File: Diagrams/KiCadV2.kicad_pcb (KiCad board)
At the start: 2 copper layers, 76.4 x 52.6 mm, 150 parts, among them J1 USB_C_Receptacle_PowerOnly_6P, J3 Screw_Terminal_01x02, J4 Screw_Terminal_01x02, U1 MT3608, U10 NC7SZ157P6X, U11 NC7SZ157P6X, U12 NC7SZ157P6X, U13 NC7SZ157P6X, U14 74LV08AT14-13, U15 HIP4080A, U16 NC7SZ157P6X, U17 MX3502S, U18 MX3502S, U19 NC7SZ157P6X, U2 74HC595, U20 NC7SZ157P6X, U22 DMHT10H032LFJ, U23 INA240A1D, U26 MX3502S, U3 NC7SZ157P6X, U30 DMHT10H032LFJ, U31 INA240A1D, U32 NC7SZ157P6X, U33 NC7SZ157P6X, U34 NC7SZ157P6X, U35 NC7SZ157P6X, U36 NC7SZ157P6X, U37 NC7SZ157P6X, U38 74LV08AT14-13, U39 HIP4080A, U4 NC7SZ157P6X, U40 MCP6002-xSN, U41 CJ432, U5 MX3502S, U6 NC7SZ157P6X, U7 DAC082S085CISDX/NOPB, U8 NC7SZ157P6X, U9 NC7SZ157P6X

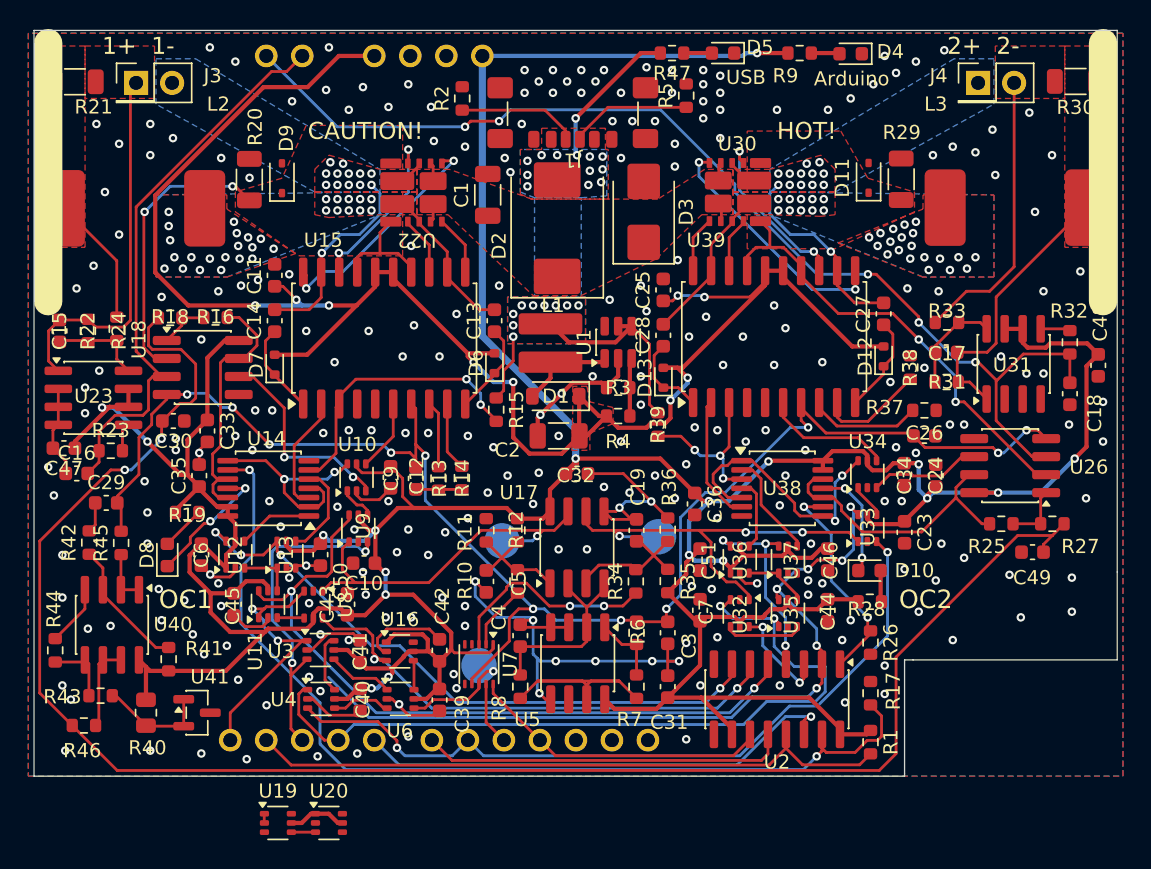
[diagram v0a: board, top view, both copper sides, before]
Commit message: Fixed AND Gate pins, added extra DAC logic Mux
DAC logic mux not yet done on PCB
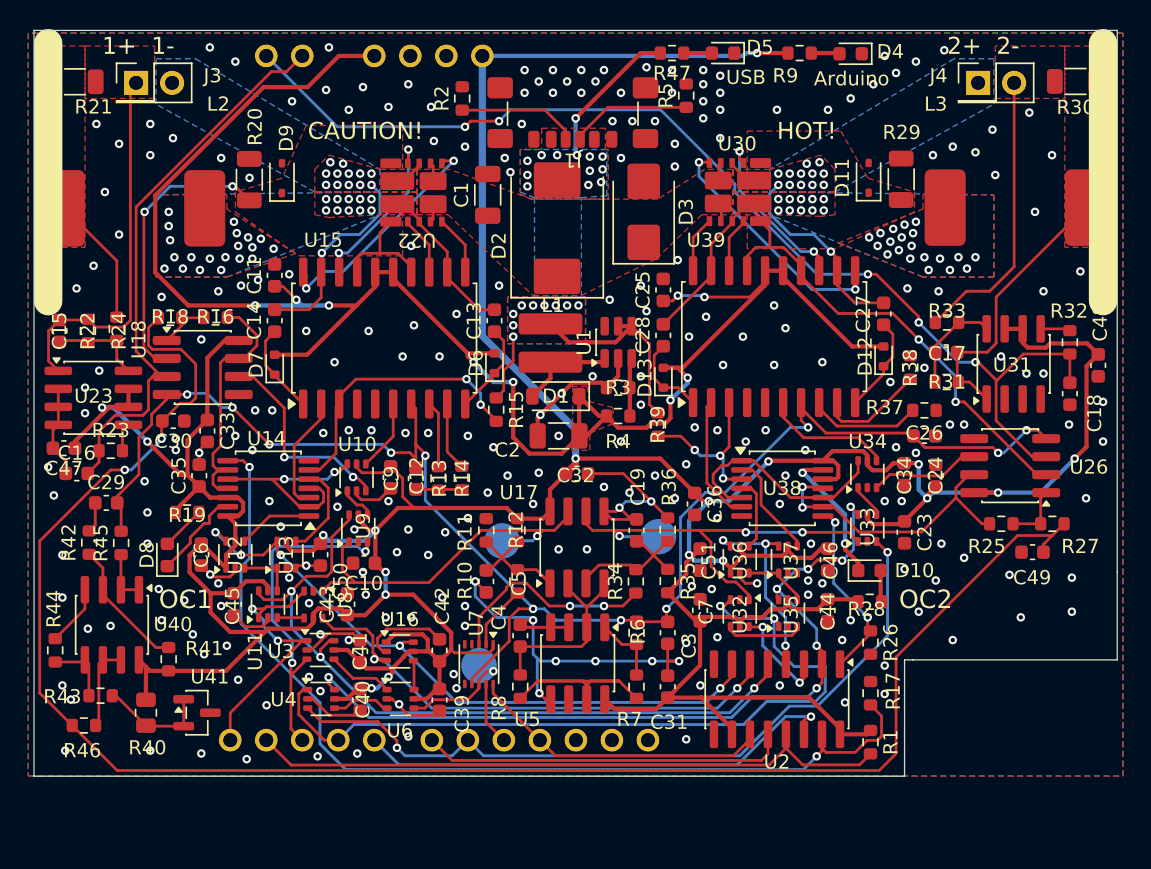
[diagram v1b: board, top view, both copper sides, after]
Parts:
- removed U19, U20: NC7SZ157P6X, Package_TO_SOT_SMD:SOT-363_SC-70-6
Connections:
- U14 pad 10: /PerCoil/~{OC1} -> /PerCoil/SignalProcessingChain/EN
- U14 pad 11: Net-(D8-K) -> /PerCoil/~{OC1}
- U14 pad 12: /PerCoil/~{OC1} -> +5V
- U14 pad 13: +5V -> Net-(D8-K)
- U14 pad 8: /PerCoil/SignalProcessingChain/EN -> /EN1
- U14 pad 9: /EN1 -> /PerCoil/~{OC1}
- U16 pad 6: /A1 -> /C1
- U3 pad 6: /S1 -> /A1
- U38 pad 10: /PerCoil1/~{OC1} -> /PerCoil1/SignalProcessingChain/EN
- U38 pad 11: Net-(D10-K) -> /PerCoil1/~{OC1}
- U38 pad 12: /PerCoil1/~{OC1} -> +5V
- U38 pad 13: +5V -> Net-(D10-K)
- U38 pad 8: /PerCoil1/SignalProcessingChain/EN -> /EN2
- U38 pad 9: /EN2 -> /PerCoil1/~{OC1}
- U4 pad 6: /S1 -> /A2
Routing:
- net /S1: track 4.18 -> 0.00 mm
- net /EN2: track 15.1 -> 12.2 mm
- net /PerCoil1/SignalProcessingChain/EN: track 19.1 -> 16.3 mm, vias 2 -> 0
- net Net-(D8-K): track 9.25 -> 6.56 mm, vias 2 -> 0
- net Net-(D10-K): track 7.97 -> 10.1 mm
- net /A1: track 50.7 -> 52.4 mm, vias 2 -> 3
- net Net-(U19-Z): track 1.70 -> 0.00 mm
- net /C1: track 44.4 -> 45.4 mm, vias 4 -> 5
- net /A2: track 56.2 -> 57.2 mm, vias 6 -> 7
- net /PerCoil1/~{OC1}: track 19.7 -> 20.5 mm, vias 0 -> 2
- net GND: track 104.9 -> 104.2 mm
- net /PerCoil/~{OC1}: track 18.3 -> 17.7 mm
